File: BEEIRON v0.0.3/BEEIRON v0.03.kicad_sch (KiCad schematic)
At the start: 3 parts, among them U1 Regulator, U2 ThermoMeter

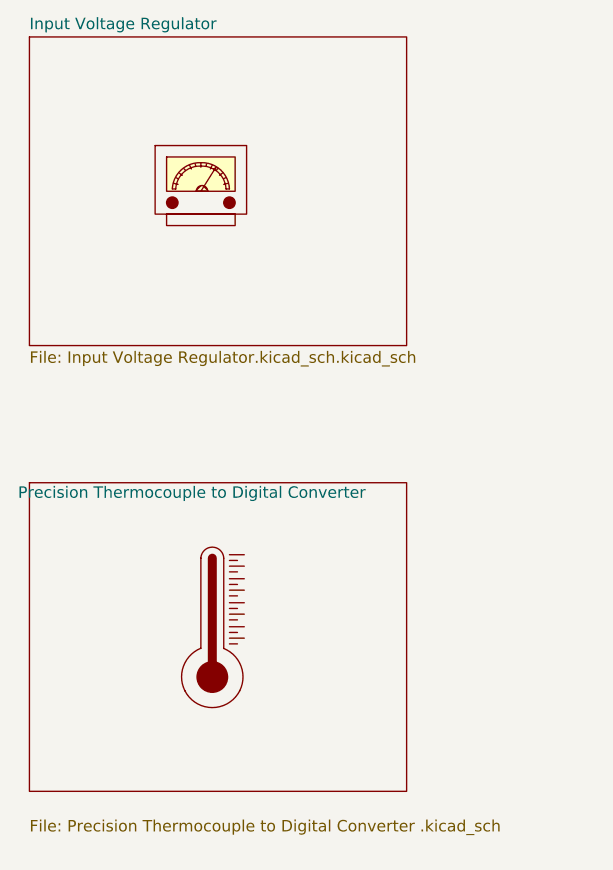
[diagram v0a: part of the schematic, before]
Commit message: minor edit in the schematics
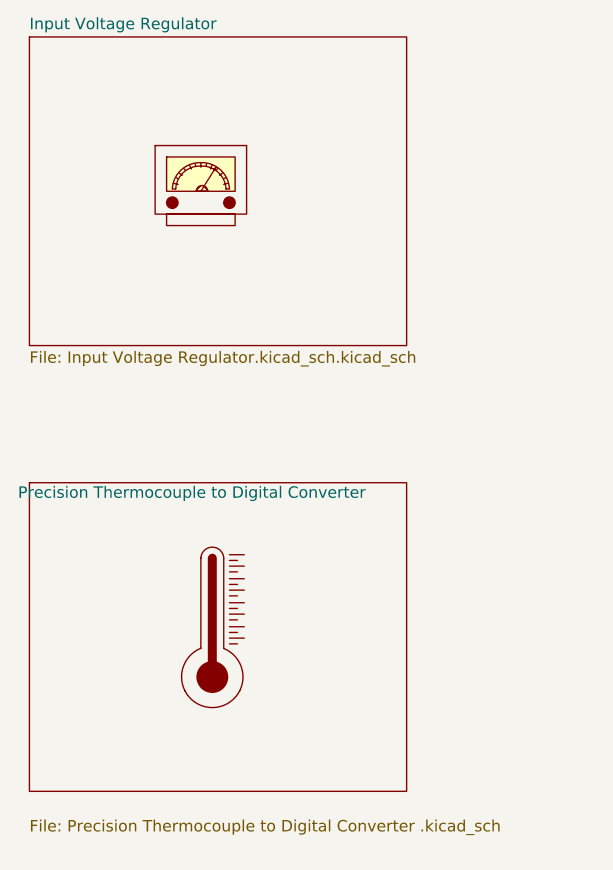
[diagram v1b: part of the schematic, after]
